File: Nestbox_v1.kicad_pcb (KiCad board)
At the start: 2 copper layers, 100 x 91 mm, 82 parts, among them P1 RX/TX, P2 TST/RST, P3 VDD/GND, P4 NFC_PWR_SEL, Q1 SFH 3605, SW1 SMD-BUTTON_2P-3.0X2.5X1.2+0.4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, U1 MSP430FR5969, U2 CR95HF, U3 TPS630250RNC, U4 RN2483, Y1 Crystal, Y2 ABM11-142-27.120MHz

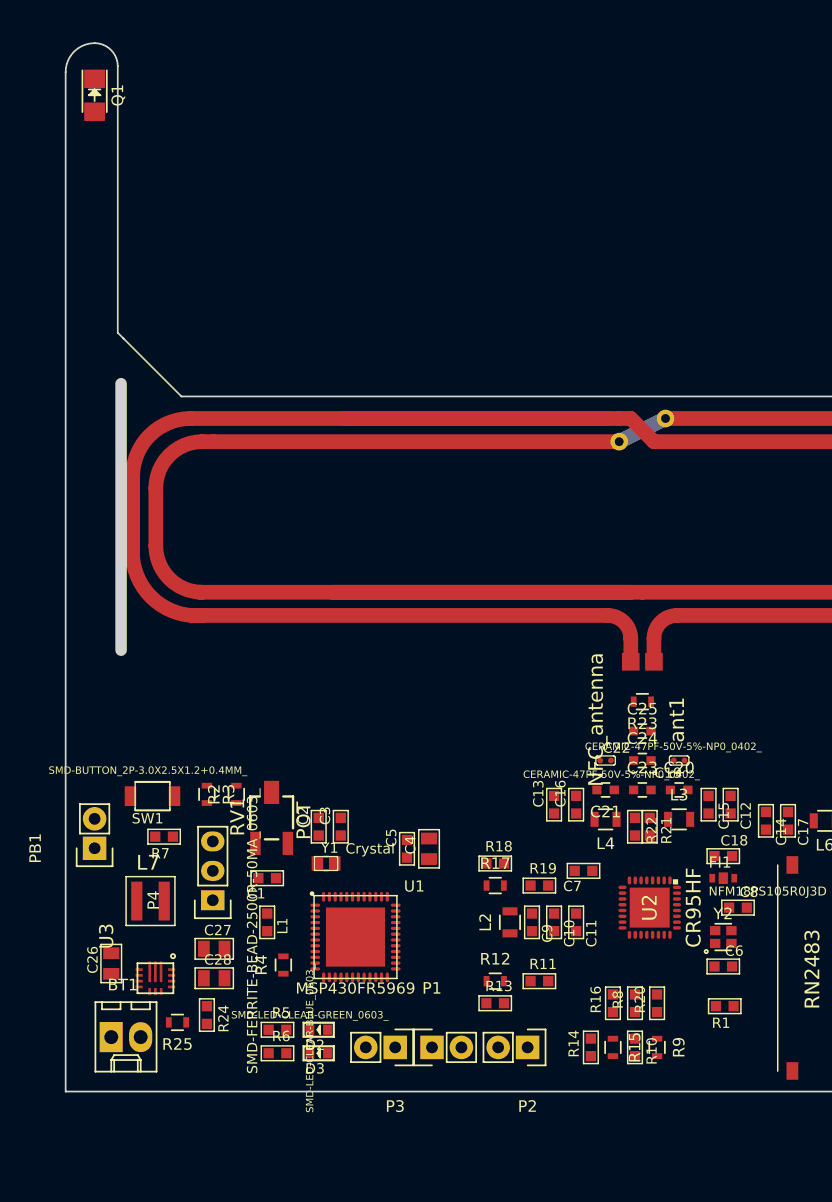
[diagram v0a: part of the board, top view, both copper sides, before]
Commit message: corrected phototransistor pins, added power jumpers & testpoints and light barrier signal access
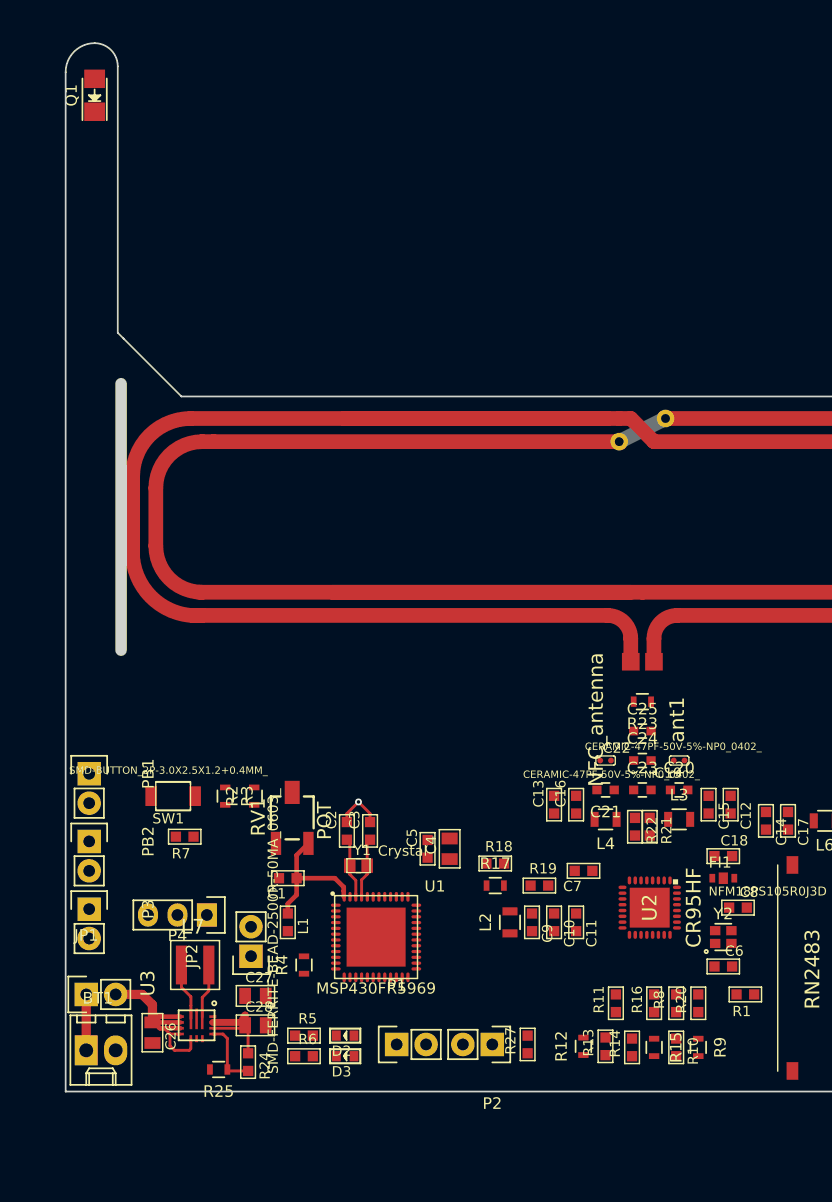
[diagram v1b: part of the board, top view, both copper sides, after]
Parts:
- added JP1: JUMPER, Socket_Strips:Socket_Strip_Straight_1x02, F.Cu at (98.6, 134.3)
- added JP2: JUMPER, Socket_Strips:Socket_Strip_Straight_1x02, F.Cu at (112.9, 131.0)
- added PB1: LIGHT_BARRIER1, Socket_Strips:Socket_Strip_Straight_1x02, F.Cu at (98.9, 115.2)
- added R27: 47K, SeeedOPL-Resistor-2016:R0603, F.Cu at (136.7, 138.6)
- L7: value XFL4020 -> XFL4020-102ME
- moved P3 29.0 mm to (98.9, 126.9), turned to 270 degrees
- moved R13 10.2 mm to (143.5, 138.8), turned to 0 degrees
- moved R12 9.46 mm to (141.6, 138.8), turned to 90 degrees
- moved C26 6.95 mm to (104.4, 137.6), turned to 0 degrees
- moved R11 6.87 mm to (144.4, 135.0), turned to 0 degrees
- moved L7 6.73 mm to (108.0, 131.7)
- moved C27 5.40 mm to (113.3, 134.4)
- moved C28 5.40 mm to (113.3, 136.9)
- moved U3 5.40 mm to (108.2, 136.9)
- moved R24 5.40 mm to (112.6, 140.1)
- moved R25 5.40 mm to (110.1, 140.8)
- moved R10 3.56 mm to (149.6, 138.8)
- moved R14 3.56 mm to (145.8, 138.8)
- moved R15 3.56 mm to (147.7, 138.8)
- moved R16 3.56 mm to (147.7, 135.0)
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- renumbered PB1 to PB2
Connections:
- net Net-(R1-Pad1) renamed /light_barrier_out
- C26 pad 1: +BATT -> Net-(C26-Pad1)
- C27 pad 1: +3V3 -> Net-(C27-Pad1)
- C28 pad 1: +3V3 -> Net-(C27-Pad1)
- R24 pad 2: +3V3 -> Net-(C27-Pad1)
- U3 pad 12: +3V3 -> Net-(C27-Pad1)
- U3 pad 13: +3V3 -> Net-(C27-Pad1)
- U3 pad 14: +3V3 -> Net-(C27-Pad1)
- U3 pad 4: +BATT -> Net-(C26-Pad1)
- U3 pad 5: +BATT -> Net-(C26-Pad1)
- U3 pad 6: +BATT -> Net-(C26-Pad1)
- U3 pad 7: +BATT -> Net-(C26-Pad1)
- U3 pad 8: +BATT -> Net-(C26-Pad1)
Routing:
- net Net-(C26-Pad1): track 0.00 -> 18.4 mm
- net /AVCC: track 0.00 -> 12.3 mm
- net Net-(C27-Pad1): track 0.00 -> 9.39 mm
- net Net-(R24-Pad1): track 0.00 -> 5.93 mm
- net Net-(C2-Pad1): track 0.00 -> 5.25 mm
- net Net-(C3-Pad1): track 0.00 -> 5.23 mm
- net Net-(L7-Pad1): track 0.00 -> 4.99 mm
- net Net-(L7-Pad2): track 0.00 -> 4.89 mm
- net +BATT: track 0.00 -> 4.83 mm
- net GND: track 0.00 -> 4.30 mm, vias 0 -> 1
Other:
- net class Default: via_drill 0.4 -> 0.3
- net class Power added: clearance 0.3, trace_width 0.4, via_dia 0.9, via_drill 0.6
- net class high_power added: clearance 0.3, trace_width 0.6, via_dia 0.9, via_drill 0.6

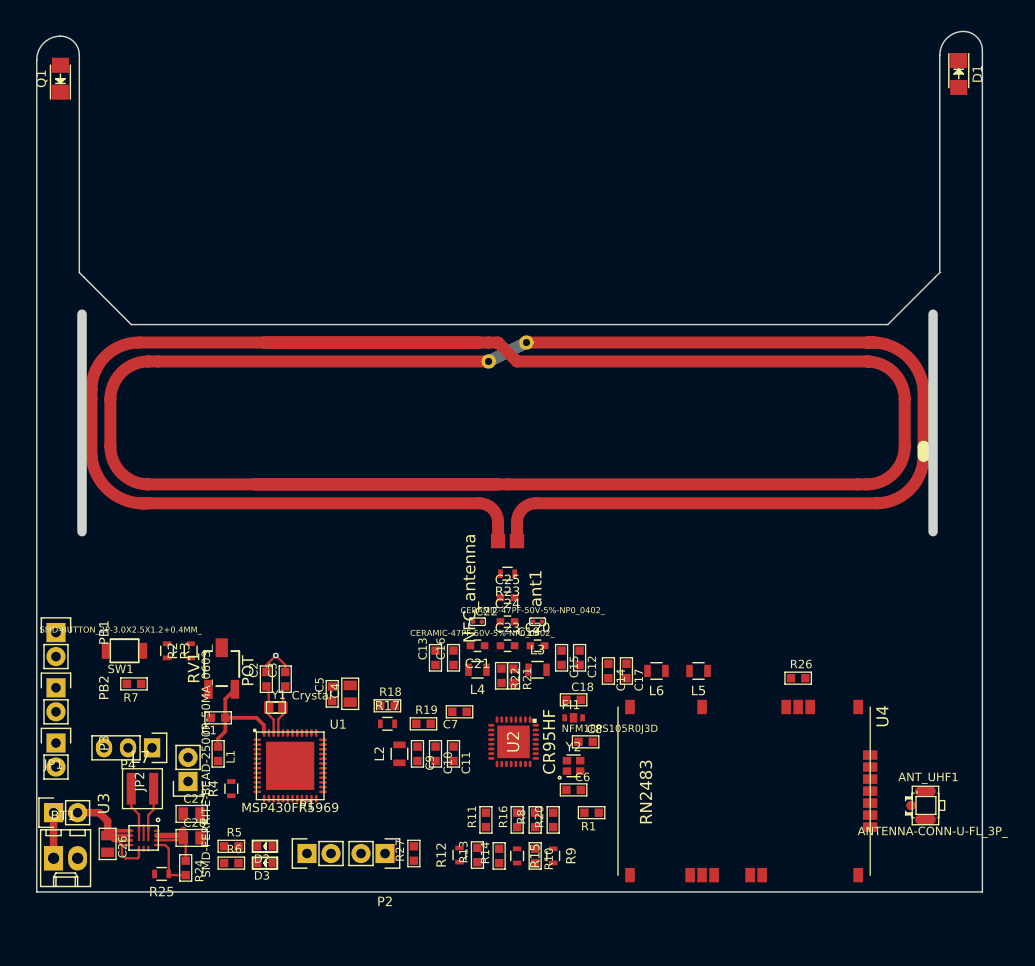
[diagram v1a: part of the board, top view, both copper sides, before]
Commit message: added second phototransistor. started routing power and analog traces
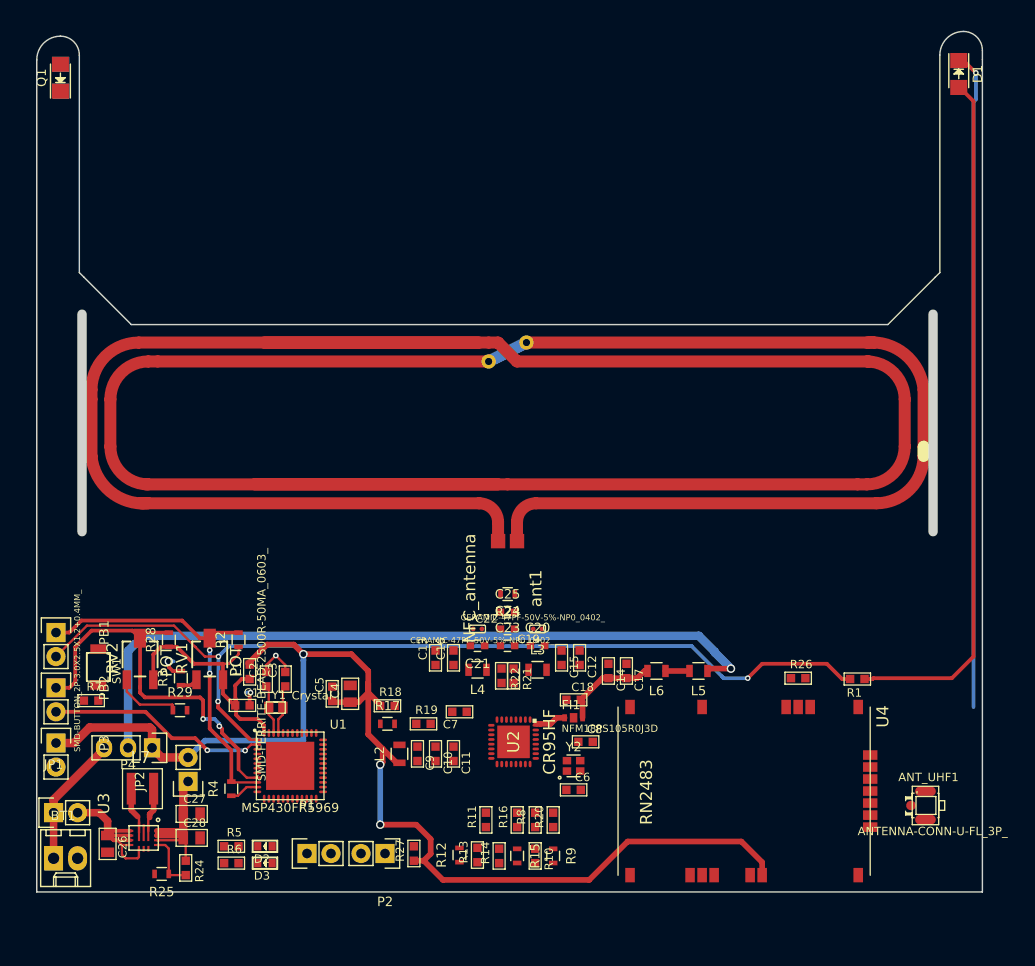
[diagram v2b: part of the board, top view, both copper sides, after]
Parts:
- added Q2: SFH 3605, Octanis3:MIDLED_phototransistor, B.Cu at (99.4, 56.6)
- added R28: R_OPTO, Resistors_SMD:R_0603, F.Cu at (110.8, 116.0)
- added R29: DNP, Resistors_SMD:R_0603, F.Cu at (112.0, 123.4)
- added RV2: POT, pot:3223G, F.Cu at (107.8, 118.0)
- D1: value SFH 4656 -> SFH 4646
- moved R1 31.5 mm to (183.6, 120.1)
- moved L1 9.29 mm to (119.4, 119.4), turned to 90 degrees
- moved R2 5.19 mm to (118.2, 116.0)
- moved R7 4.86 mm to (102.6, 122.4), turned to 270 degrees
- moved SW1 3.25 mm to (103.4, 118.9), turned to 270 degrees
- moved R3 3.24 mm to (112.1, 120.1), turned to 90 degrees
- moved C1 2.89 mm to (118.6, 122.9), turned to 90 degrees
- moved R23 2.16 mm to (146.7, 111.2)
- moved RV1 1.63 mm to (115.2, 118.0)
- moved C25 1.52 mm to (146.7, 113.1)
- moved C19 0.76 mm to (149.8, 114.8)
- moved C22 0.76 mm to (143.5, 114.8)
- moved C24 0.76 mm to (146.7, 114.8)
- moved Q1 0.11 mm to (99.4, 56.6)
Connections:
- net Net-(PB1-Pad1) renamed /light_barrier1_in
- net Net-(PB2-Pad1) renamed /light_barrier2_in
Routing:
- net +3V3: track 0.00 -> 130.6 mm, vias 0 -> 3
- net /light_barrier_out: track 0.00 -> 100.5 mm, vias 0 -> 3
- net VDDA: track 0.00 -> 78.7 mm, vias 0 -> 1
- net GND: track 4.30 -> 78.3 mm, vias 1 -> 4
- net Net-(D1-Pad2): track 0.00 -> 73.4 mm
- net /light_barrier2_in: track 0.00 -> 41.9 mm, vias 0 -> 2
- net /light_barrier1_in: track 0.00 -> 40.0 mm, vias 0 -> 2
- net Net-(PB2-Pad2): track 0.00 -> 23.2 mm, vias 0 -> 2
- net /AVCC: track 12.3 -> 29.8 mm
- net Net-(C14-Pad2): track 0.00 -> 10.3 mm
- net +BATT: track 4.83 -> 13.9 mm
- net Net-(C27-Pad1): track 9.39 -> 18.2 mm
- net Net-(R29-Pad1): track 0.00 -> 7.62 mm
- net Net-(FI1-Pad1): track 0.00 -> 3.27 mm
- net Net-(R4-Pad1): track 0.00 -> 3.13 mm
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
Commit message: finished big part of the routing
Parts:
- added C29: CERAMIC-100NF-50V-10%-X7R_0603_, SeeedOPL-Capacitor-2016:C0603, F.Cu at (120.5, 137.4)
- added R30: SMD-RES-10K-1%-1_10W_0603_, SeeedOPL-Resistor-2016:R0603, F.Cu at (120.5, 135.7)
- moved P1 1.93 mm to (127.4, 138.7), turned to 180 degrees
- moved D2 1.41 mm to (120.8, 139.2)
- moved D3 1.41 mm to (120.8, 141.0)
- moved R5 1.41 mm to (117.2, 139.2)
- moved R6 1.41 mm to (117.2, 141.0)
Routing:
- net GND: track 78.3 -> 193.0 mm, vias 4 -> 24
- net LORA_RST_N: track 0.00 -> 63.7 mm, vias 0 -> 2
- net /light_barrier1_in: track 40.0 -> 102.1 mm
- net /light_barrier2_in: track 41.9 -> 101.9 mm, vias 2 -> 3
- net LORA_RX: track 0.00 -> 50.6 mm, vias 0 -> 2
- net LORA_TX: track 0.00 -> 45.6 mm, vias 0 -> 2
- net +3V3: track 130.6 -> 171.1 mm, vias 3 -> 5
- net Net-(R30-Pad1): track 0.00 -> 33.0 mm, vias 0 -> 2
- net NFC_IRQ_N: track 0.00 -> 26.5 mm, vias 0 -> 3
- net SPI_NFC_SEL_N: track 0.00 -> 22.7 mm, vias 0 -> 2
- net NFC_WAKEUP_N: track 0.00 -> 21.7 mm, vias 0 -> 2
- net SPI_SCK: track 0.00 -> 21.4 mm
- net SPI_MISO: track 0.00 -> 20.3 mm
- net SPI_MOSI: track 0.00 -> 20.3 mm
- net Net-(C21-Pad1): track 0.00 -> 19.2 mm
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
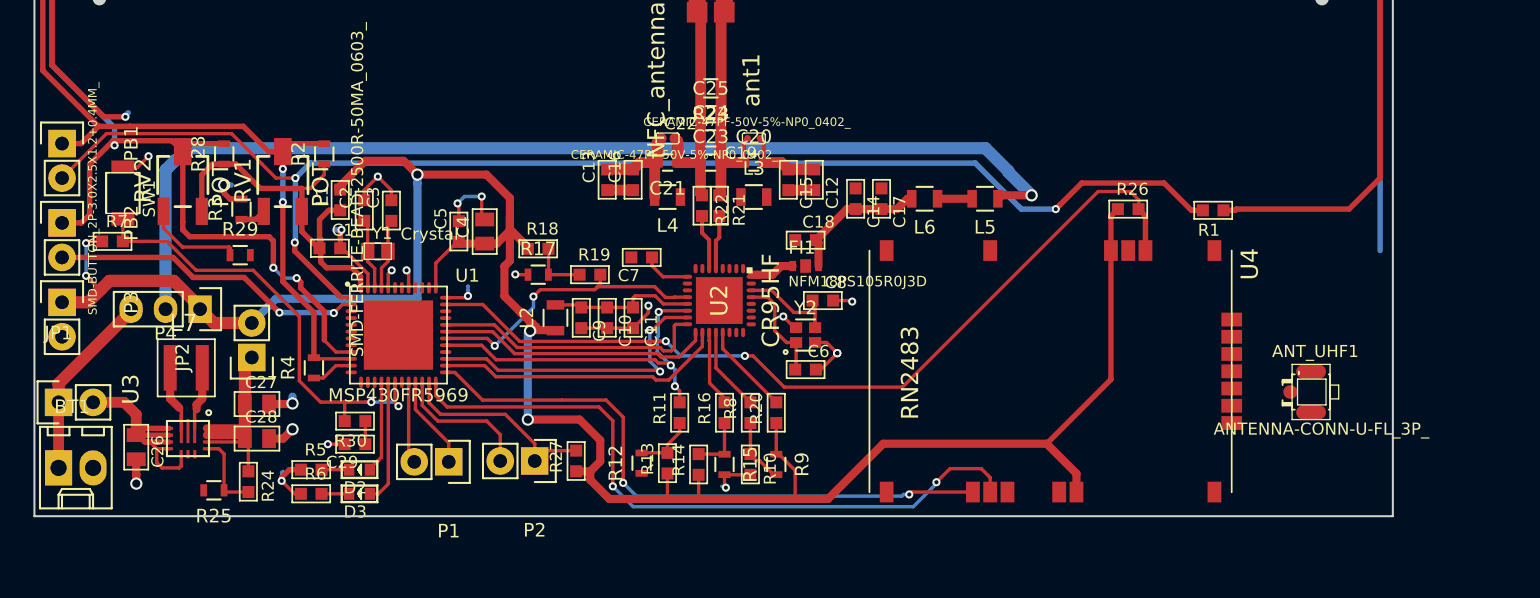
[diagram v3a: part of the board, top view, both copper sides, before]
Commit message: routing done. missing: top ground plane, stitching vias
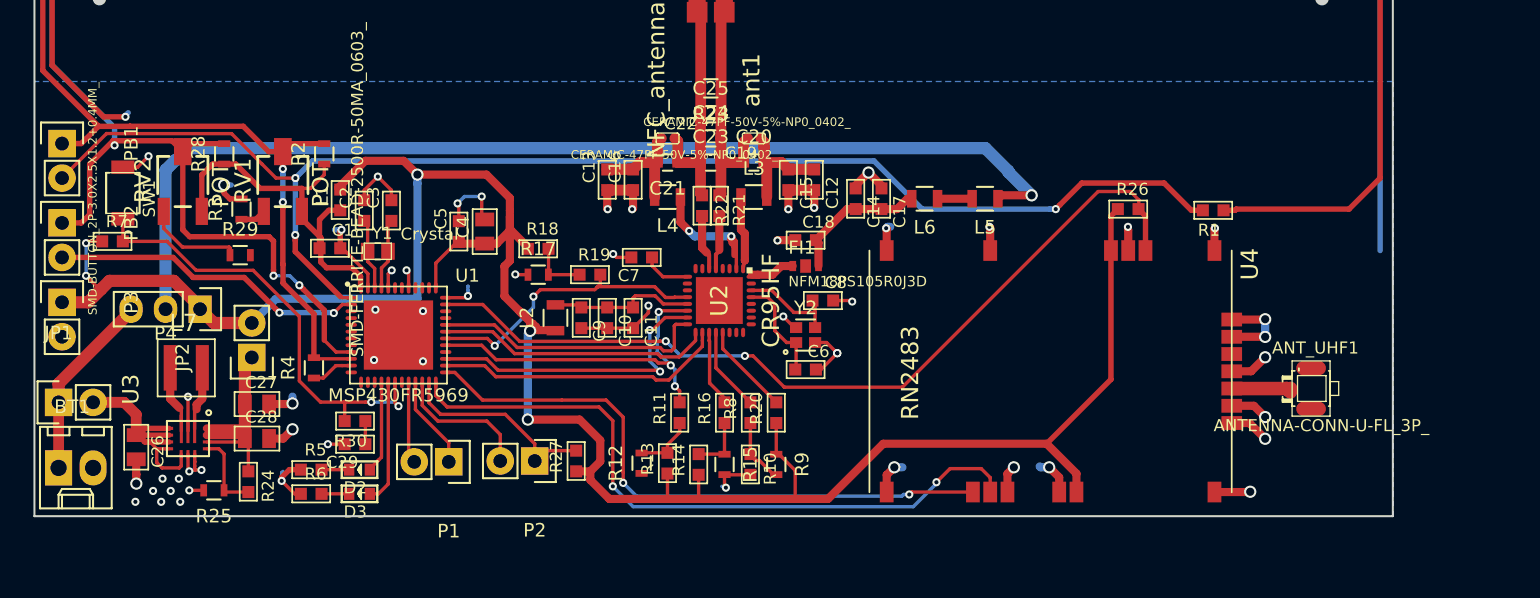
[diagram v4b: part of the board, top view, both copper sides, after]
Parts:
- moved ANT_UHF1 0.26 mm to (190.8, 133.3)
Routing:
- net GND: track 193.0 -> 244.0 mm, vias 24 -> 59
- net Net-(L4-Pad1): track 0.00 -> 10.5 mm, vias 0 -> 2
- net Net-(L3-Pad1): track 0.00 -> 5.41 mm
- net Net-(ANT_UHF1-PadD): track 0.00 -> 4.42 mm
- net Net-(C12-Pad1): track 5.80 -> 9.42 mm
- net /light_barrier_out: track 100.8 -> 101.5 mm
- added copper zone on B.Cu, net GND
